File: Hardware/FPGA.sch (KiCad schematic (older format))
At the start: 17 parts, among them U501 W25Q128JVxxM, U502 ICE40UP5K-SG48, U503 Crystal Oscillator, U504 USBLC6-2

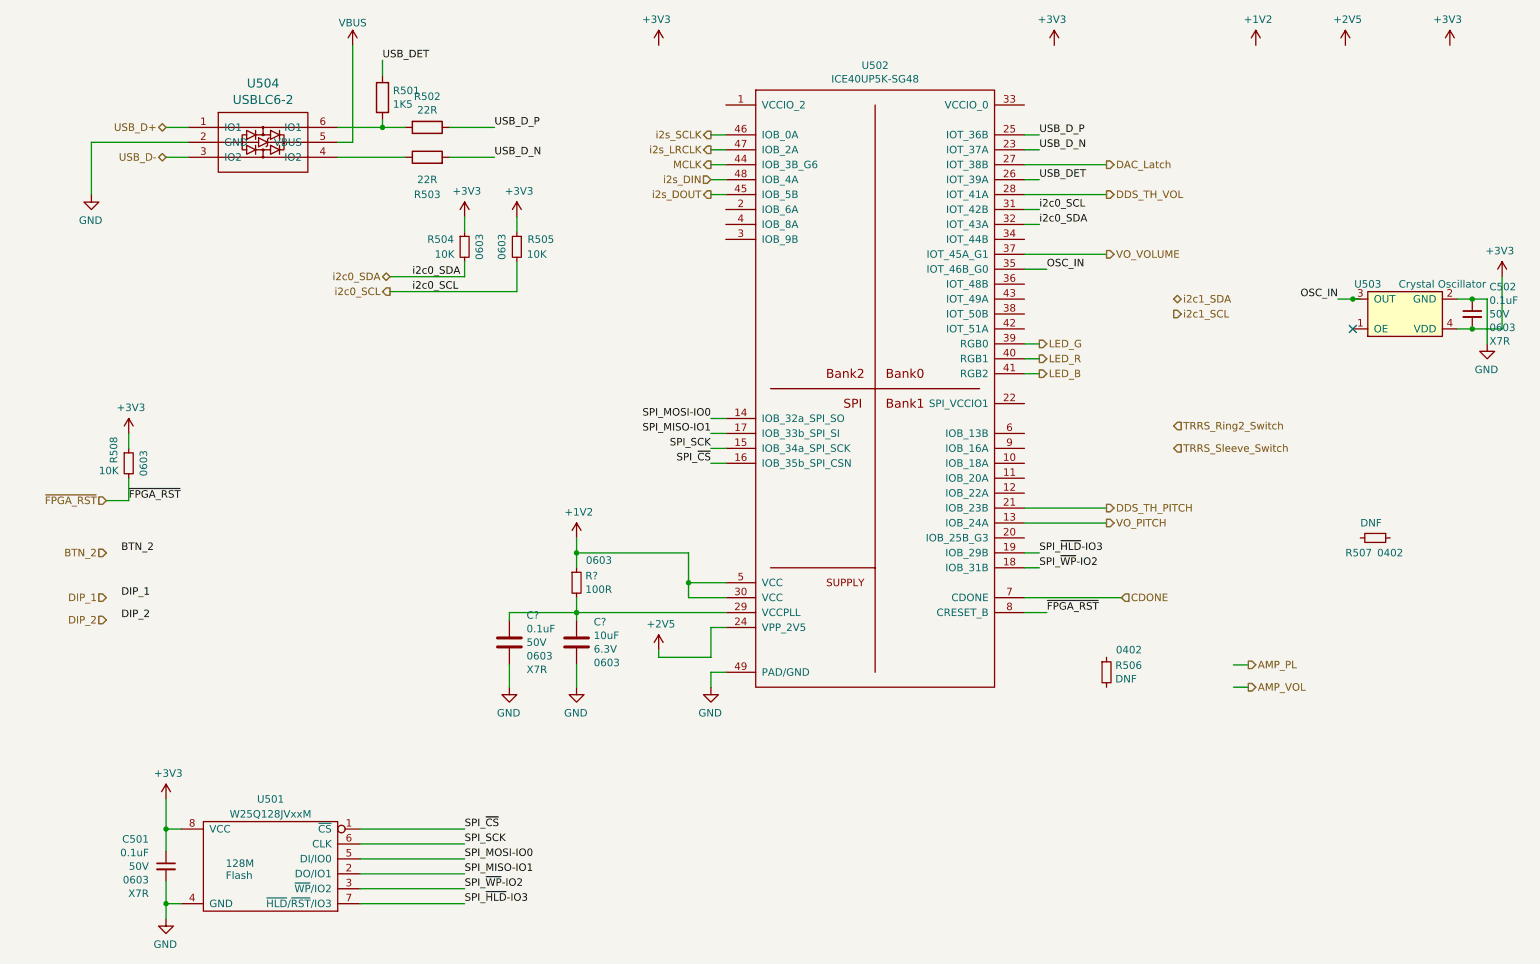
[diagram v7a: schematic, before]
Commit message: Schematic has proposed pin mapping on FPGA.
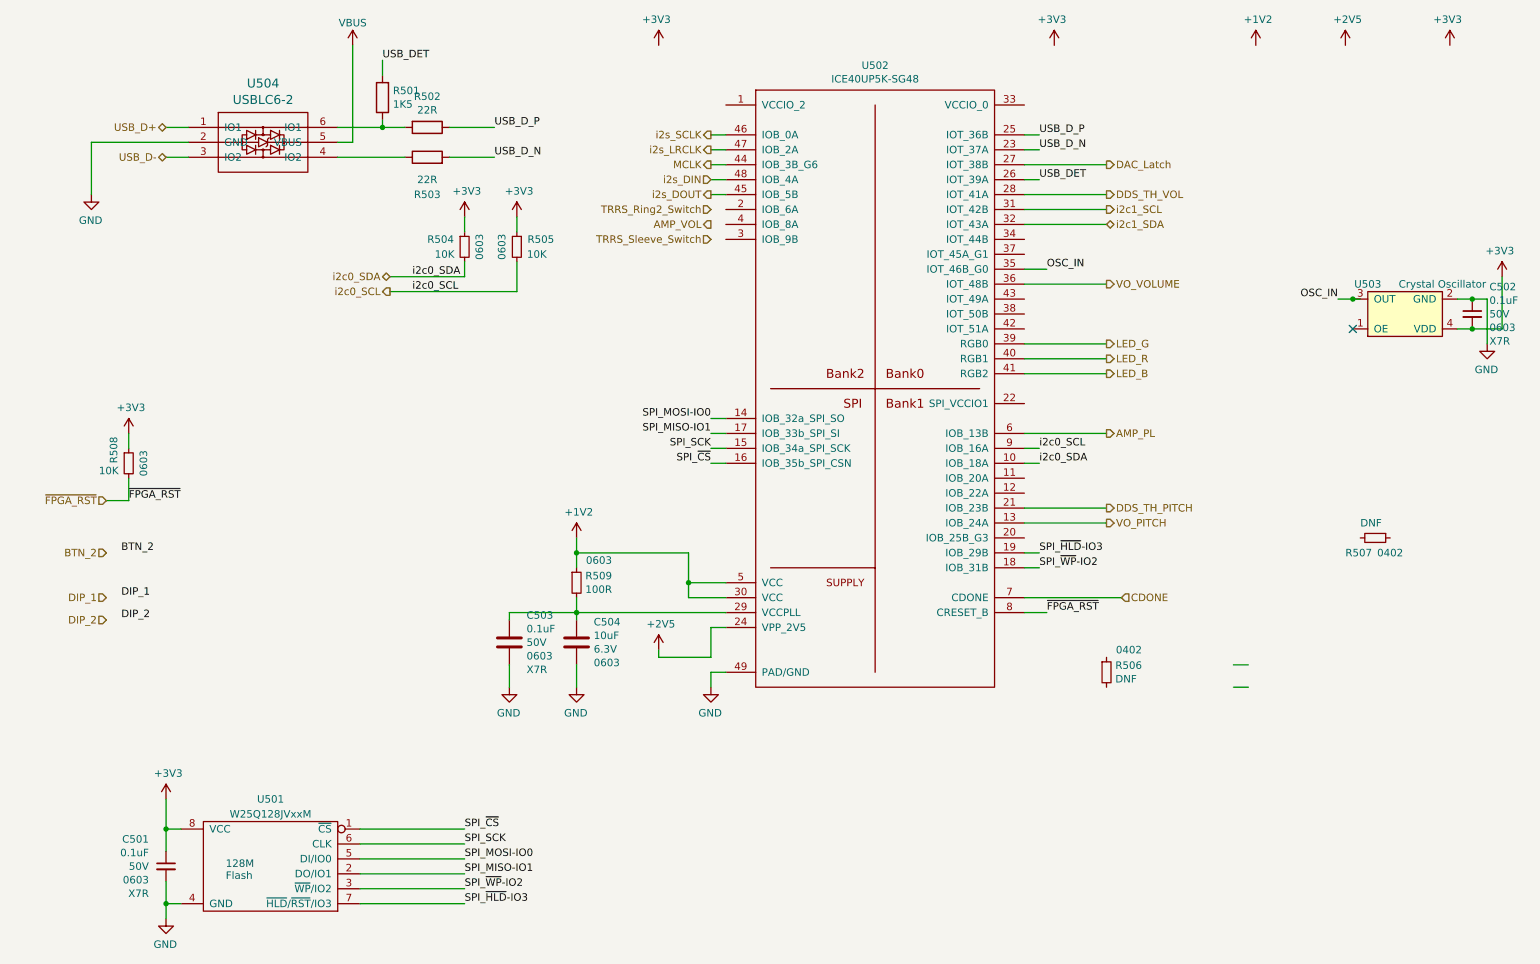
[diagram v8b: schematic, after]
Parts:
- gave numbers to parts that had none: 3
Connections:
- wire segments 91 -> 94
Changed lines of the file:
@@
 	1    0    0    -1
 $EndComp
-Text HLabel 7550 3050 2    50   Output ~ 0
+Text HLabel 8000 3050 2    50   Output ~ 0
 LED_B
-Text HLabel 7550 2850 2    50   Output ~ 0
+Text HLabel 8000 2850 2    50   Output ~ 0
 LED_G
-Text HLabel 7550 2950 2    50   Output ~ 0
+Text HLabel 8000 2950 2    50   Output ~ 0
 LED_R
 Wire Wire Line
-	7450 2850 7550 2850
-Wire Wire Line
-	7450 2950 7550 2950
-Wire Wire Line
-	7450 3050 7550 3050
+	7450 2850 8000 2850
+Wire Wire Line
+	7450 2950 8000 2950
+Wire Wire Line
+	7450 3050 8000 3050
 Text HLabel 3200 2400 0    50   BiDi ~ 0
 i2c0_SDA
@@
 Text HLabel 8000 1650 2    50   Output ~ 0
 DAC_Latch
-Text HLabel 8000 2250 2    50   Output ~ 0
+Text HLabel 8000 2450 2    50   Output ~ 0
 VO_VOLUME
 Text HLabel 8000 4050 2    50   Output ~ 0
@@
 	0    1    1    0
 $EndComp
-Text HLabel 8950 5150 2    50   Output ~ 0
+Text HLabel 5350 2050 0    50   Output ~ 0
 AMP_VOL
 Wire Wire Line
 	8950 5150 8850 5150
-Text HLabel 8950 5000 2    50   Output ~ 0
+Text HLabel 8000 3450 2    50   Output ~ 0
 AMP_PL
 Wire Wire Line
@@
 P 4450 4450
 AR Path="/611E335F/6171709C" Ref="R?"  Part="1"
-AR Path="/611E3335/6171709C" Ref="R?"  Part="1"
-F 0 "R?" H 4509 4496 50  0000 L CNN
+AR Path="/611E3335/6171709C" Ref="R509"  Part="1"
+F 0 "R509" H 4509 4496 50  0000 L CNN
 F 1 "100R" H 4509 4405 50  0000 L CNN
 F 2 "Resistor_SMD:R_0603_1608Metric" V 4380 4450 50  0001 C CNN
@@
 P 4450 4850
 AR Path="/611E335F/61722BBF" Ref="C?"  Part="1"
-AR Path="/611E3335/61722BBF" Ref="C?"  Part="1"
-F 0 "C?" H 4565 4987 50  0000 L CNN
+AR Path="/611E3335/61722BBF" Ref="C504"  Part="1"
+F 0 "C504" H 4565 4987 50  0000 L CNN
 F 1 "10uF" H 4565 4896 50  0000 L CNN
 F 2 "Capacitor_SMD:C_0603_1608Metric" H 4488 4700 50  0001 C CNN
@@
 P 4000 4850
 AR Path="/611E335F/61722BCA" Ref="C?"  Part="1"
-AR Path="/611E3335/61722BCA" Ref="C?"  Part="1"
-F 0 "C?" H 4115 5032 50  0000 L CNN
+AR Path="/611E3335/61722BCA" Ref="C503"  Part="1"
+F 0 "C503" H 4115 5032 50  0000 L CNN
 F 1 "0.1uF" H 4115 4941 50  0000 L CNN
 F 2 "Capacitor_SMD:C_0603_1608Metric" H 4038 4700 50  0001 C CNN
@@
 $EndComp
 $Comp
-L power:GND #PWR?
+L power:GND #PWR0161
 U 1 1 61726268
 P 5350 5150
-F 0 "#PWR?" H 5350 4900 50  0001 C CNN
+F 0 "#PWR0161" H 5350 4900 50  0001 C CNN
 F 1 "GND" H 5355 4977 50  0000 C CNN
 F 2 "" H 5350 5150 50  0001 C CNN
@@
 AR Path="/6123BB15/61733590" Ref="#PWR?"  Part="1"
 AR Path="/611E335F/61733590" Ref="#PWR?"  Part="1"
-AR Path="/611E3335/61733590" Ref="#PWR?"  Part="1"
-F 0 "#PWR?" H 4450 4000 50  0001 C CNN
+AR Path="/611E3335/61733590" Ref="#PWR0162"  Part="1"
+F 0 "#PWR0162" H 4450 4000 50  0001 C CNN
 F 1 "+1V2" H 4465 4323 50  0000 C CNN
 F 2 "" H 4450 4150 50  0001 C CNN
@@
 	4000 4650 4450 4650
 $Comp
-L power:GND #PWR?
+L power:GND #PWR0163
 U 1 1 617389F4
 P 4450 5150
-F 0 "#PWR?" H 4450 4900 50  0001 C CNN
+F 0 "#PWR0163" H 4450 4900 50  0001 C CNN
 F 1 "GND" H 4455 4977 50  0000 C CNN
 F 2 "" H 4450 5150 50  0001 C CNN
@@
 	4450 4550 4450 4650
 $Comp
-L power:GND #PWR?
+L power:GND #PWR0164
 U 1 1 6173B232
 P 4000 5150
-F 0 "#PWR?" H 4000 4900 50  0001 C CNN
+F 0 "#PWR0164" H 4000 4900 50  0001 C CNN
 F 1 "GND" H 4005 4977 50  0000 C CNN
 F 2 "" H 4000 5150 50  0001 C CNN
@@
 AR Path="/6123BB15/617476D3" Ref="#PWR?"  Part="1"
 AR Path="/611E335F/617476D3" Ref="#PWR?"  Part="1"
-AR Path="/611E3335/617476D3" Ref="#PWR?"  Part="1"
-F 0 "#PWR?" H 5000 4750 50  0001 C CNN
+AR Path="/611E3335/617476D3" Ref="#PWR0165"  Part="1"
+F 0 "#PWR0165" H 5000 4750 50  0001 C CNN
 F 1 "+2V5" H 5015 5073 50  0000 C CNN
 F 2 "" H 5000 4900 50  0001 C CNN
@@
 AR Path="/6123BB15/6174C4EC" Ref="#PWR?"  Part="1"
 AR Path="/611E335F/6174C4EC" Ref="#PWR?"  Part="1"
-AR Path="/611E3335/6174C4EC" Ref="#PWR?"  Part="1"
-F 0 "#PWR?" H 9000 700 50  0001 C CNN
+AR Path="/611E3335/6174C4EC" Ref="#PWR0166"  Part="1"
+F 0 "#PWR0166" H 9000 700 50  0001 C CNN
 F 1 "+1V2" H 9015 1023 50  0000 C CNN
 F 2 "" H 9000 850 50  0001 C CNN
@@
 AR Path="/6123BB15/6174CE7E" Ref="#PWR?"  Part="1"
 AR Path="/611E335F/6174CE7E" Ref="#PWR?"  Part="1"
-AR Path="/611E3335/6174CE7E" Ref="#PWR?"  Part="1"
-F 0 "#PWR?" H 9600 700 50  0001 C CNN
+AR Path="/611E3335/6174CE7E" Ref="#PWR0167"  Part="1"
+F 0 "#PWR0167" H 9600 700 50  0001 C CNN
 F 1 "+2V5" H 9615 1023 50  0000 C CNN
 F 2 "" H 9600 850 50  0001 C CNN
@@
 $EndComp
 $Comp
-L power:+3V3 #PWR?
+L power:+3V3 #PWR0168
 U 1 1 6174EEF9
 P 10300 850
-F 0 "#PWR?" H 10300 700 50  0001 C CNN
+F 0 "#PWR0168" H 10300 700 50  0001 C CNN
 F 1 "+3V3" H 10315 1023 50  0000 C CNN
 F 2 "" H 10300 850 50  0001 C CNN
@@
 $EndComp
 $Comp
-L power:+3V3 #PWR?
+L power:+3V3 #PWR0169
 U 1 1 6174FC67
 P 5000 850
-F 0 "#PWR?" H 5000 700 50  0001 C CNN
+F 0 "#PWR0169" H 5000 700 50  0001 C CNN
 F 1 "+3V3" H 5015 1023 50  0000 C CNN
 F 2 "" H 5000 850 50  0001 C CNN
@@
 	7450 1450 7550 1450
 $Comp
-L power:+3V3 #PWR?
+L power:+3V3 #PWR0170
 U 1 1 61762CA8
 P 7650 850
-F 0 "#PWR?" H 7650 700 50  0001 C CNN
+F 0 "#PWR0170" H 7650 700 50  0001 C CNN
 F 1 "+3V3" H 7665 1023 50  0000 C CNN
 F 2 "" H 7650 850 50  0001 C CNN
@@
 Text Label 1400 4250 0    50   ~ 0
 BTN_2
-Text HLabel 8450 2650 2    50   Output ~ 0
+Text HLabel 8000 1950 2    50   Output ~ 0
 i2c1_SCL
-Text HLabel 8450 2550 2    50   BiDi ~ 0
+Text HLabel 8000 2050 2    50   BiDi ~ 0
 i2c1_SDA
 Text HLabel 5350 1750 0    50   Input ~ 0
@@
 Text Label 3350 2500 0    50   ~ 0
 i2c0_SCL
-Text Label 7550 2050 0    50   ~ 0
-i2c0_SDA
-Text Label 7550 1950 0    50   ~ 0
-i2c0_SCL
-Wire Wire Line
-	7450 1950 7550 1950
-Wire Wire Line
-	7450 2050 7550 2050
 Wire Wire Line
 	8000 4050 7450 4050
 Wire Wire Line
-	8000 2250 7450 2250
+	8000 2450 7450 2450
 Wire Wire Line
 	8000 1650 7450 1650
@@
 Wire Wire Line
 	8000 1850 7450 1850
-Text HLabel 8450 3400 2    50   Input ~ 0
+Text HLabel 5350 1950 0    50   Input ~ 0
 TRRS_Ring2_Switch
-Text HLabel 8450 3550 2    50   Input ~ 0
+Text HLabel 5350 2150 0    50   Input ~ 0
 TRRS_Sleeve_Switch
+Text Label 7550 3650 0    50   ~ 0
+i2c0_SDA
+Text Label 7550 3550 0    50   ~ 0
+i2c0_SCL
+Wire Wire Line
+	7550 3650 7450 3650
+Wire Wire Line
+	7550 3550 7450 3550
+Wire Wire Line
+	8000 3450 7450 3450
+Wire Wire Line
+	7450 2050 8000 2050
+Wire Wire Line
+	7450 1950 8000 1950
 $EndSCHEMATC
